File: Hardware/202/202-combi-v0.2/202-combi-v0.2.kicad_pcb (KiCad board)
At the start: 6 copper layers, 64 x 33 mm, 35 parts, among them J1 DM3CS-SF_HIR, P3 LEFT-201, P4 RIGHT-201, P8 202-SMART-CAM-P, U1 TXS0104EPWR, U2 TXS0104EPWR, U3 ASE-24.000MHZ-LC-T2, U4 Smart_Cam_Expander_MSP430FR23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, U5 TCA9534PWR, U6 TPS79628DCQ

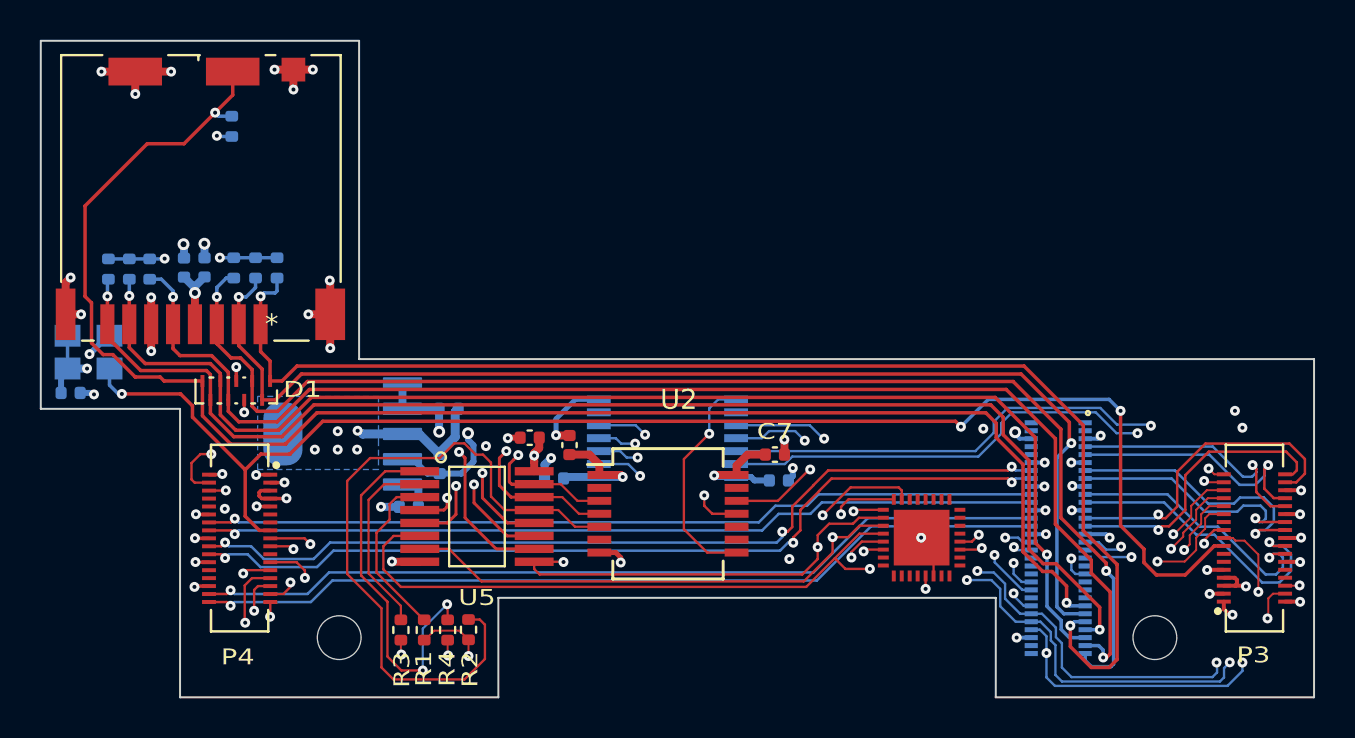
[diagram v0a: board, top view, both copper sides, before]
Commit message: Add files via upload
- PCB is converted to 6-layer board
- Differential pairs are routed and matched
- Footprint of the LDO is changed to DFN (TPS79628DRBT is in use now)
- Small changes which were causing DRC errors where corrected in Ziloo footprint library.
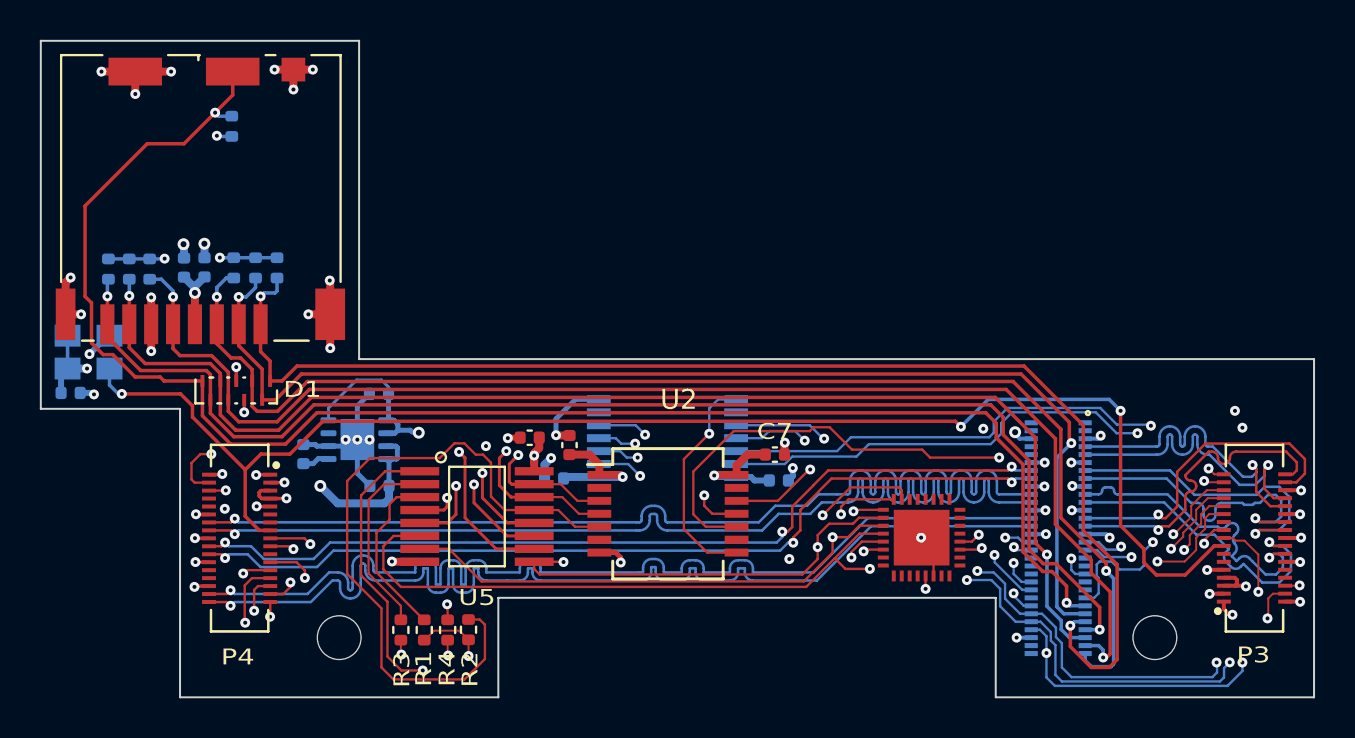
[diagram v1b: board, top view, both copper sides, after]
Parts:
- U6: value TPS79628DCQ -> TPS79628DRBT; footprint Ziloo:SOT127P706X180-6N -> Ziloo:DFN-8-1EP_3x3mm_P0.65mm_EP1.7x2.05mm
- moved C20 5.93 mm to (66.2, 75.8), turned to 90 degrees
- moved C19 3.58 mm to (70.0, 72.8), turned to 180 degrees
- moved C21 3.22 mm to (70.0, 77.4), turned to 180 degrees
- moved U6 0.79 mm to (68.9, 75.0)
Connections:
- U6 pad 3: GND -> +2V8
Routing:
- net /SYS_EX_nINT: track 0.00 -> 44.0 mm, vias 0 -> 2
- net /CSI_R_RX_D0_N: track 42.1 -> 54.0 mm
- net /CSI_R_RX_D0_P: track 42.1 -> 54.0 mm
- net /CSI_R_RX_CLK_N: track 43.1 -> 54.1 mm
- net /CSI_R_RX_CLK_P: track 43.1 -> 54.1 mm
- net +3.3V: track 119.4 -> 124.0 mm
- net /CSI_L_RX_D1_N: track 12.6 -> 15.8 mm
- net /CSI_L_RX_D2_P: track 13.0 -> 15.8 mm
- net /CSI_L_RX_D2_N: track 13.0 -> 15.8 mm
- net +2V8: track 67.7 -> 69.8 mm
- net /CSI_L_RX_D0_P: track 14.0 -> 16.0 mm
- net /CSI_L_RX_D1_P: track 14.0 -> 15.9 mm
- net /CSI_L_RX_CLK_N: track 14.7 -> 15.9 mm
- net /CSI_L_RX_D0_N: track 15.3 -> 16.1 mm
- net Net-(C20-Pad1): track 1.92 -> 1.38 mm
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- removed copper zone on B.Cu, net GND
